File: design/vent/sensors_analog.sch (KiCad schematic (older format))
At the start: 11 parts, among them J16 Conn_01x02, J17 Conn_01x02, J18 Conn_01x03, J19 Conn_01x02, J20 Conn_01x02, U11 SPU01M-15

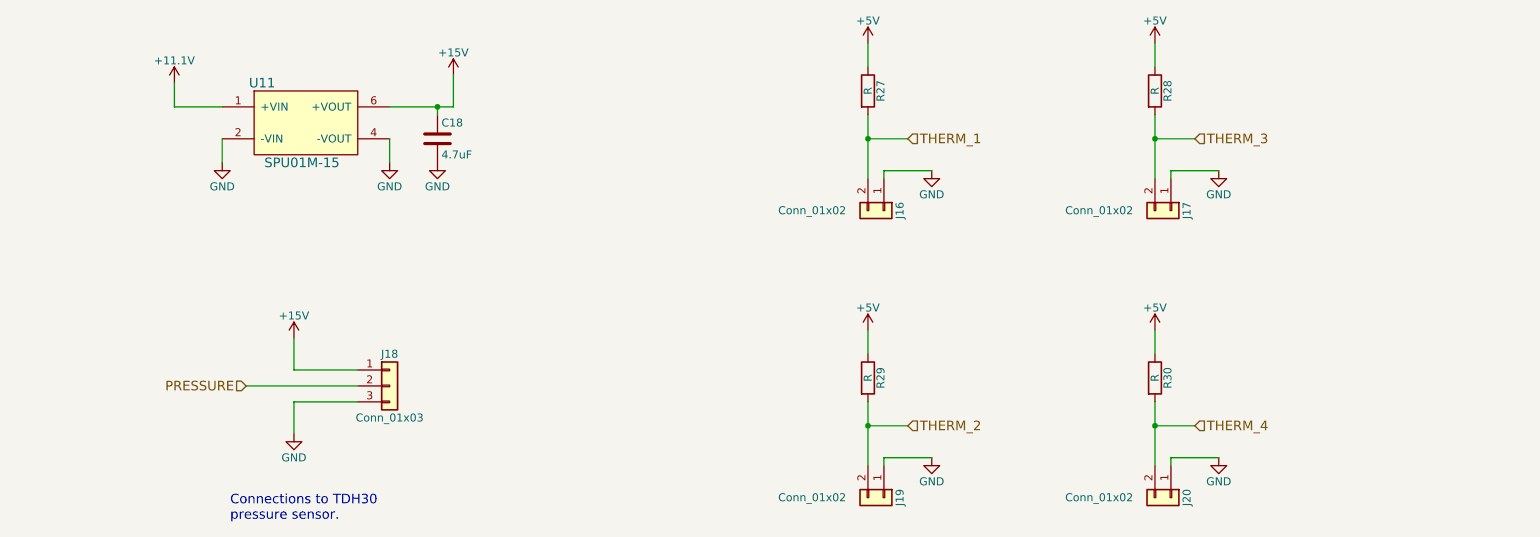
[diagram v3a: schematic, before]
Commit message: Merge control power and analog sensor connectors
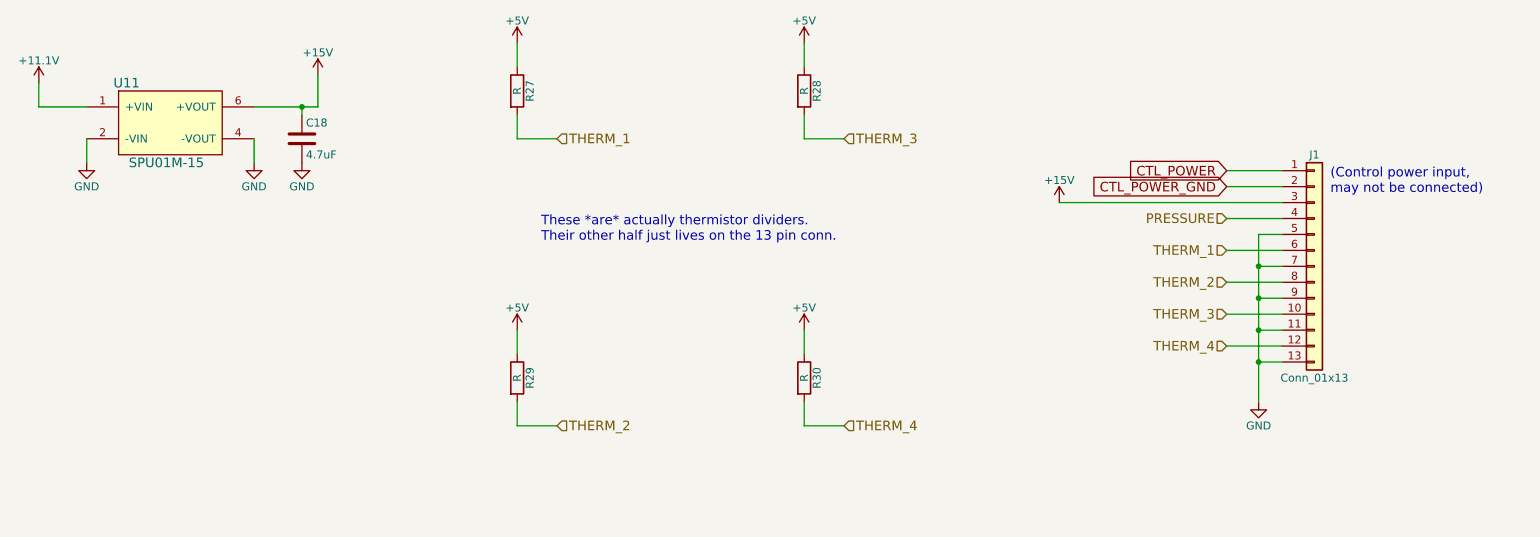
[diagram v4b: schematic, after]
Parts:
- removed J16, J17, J19, J20: Conn_01x02, Connectors_Phoenix:PhoenixContact_MCV-G_02x3.50mm_Vertical, symbol Conn_01x02
- removed J18: Conn_01x03, symbol Conn_01x03
- added J1: Conn_01x13, symbol Conn_01x13
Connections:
- net +15V: now also J1.3 (Pin_3)
- net GND: now also J1.11 (Pin_11), J1.13 (Pin_13), J1.5 (Pin_5), J1.7 (Pin_7), J1.9 (Pin_9)
- net PRESSURE: now also J1.4 (Pin_4)
- net THERM_1: now also J1.6 (Pin_6)
- net THERM_2: now also J1.8 (Pin_8)
- net THERM_3: now also J1.10 (Pin_10)
- net THERM_4: now also J1.12 (Pin_12)
- new net CTL_POWER: J1.1 (Pin_1)
- new net CTL_POWER_GND: J1.2 (Pin_2)
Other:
- note added: "(Control power input,\nmay not be connected)"
- note added: "These *are* actually thermistor dividers.\nTheir other half just lives on the 13 pin conn."
- note removed: "Connections to TDH30\npressure sensor."
- moved on the sheet: C18, R27, R28, R29, R30, U11

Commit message: Break out I2C lines on dsub connector
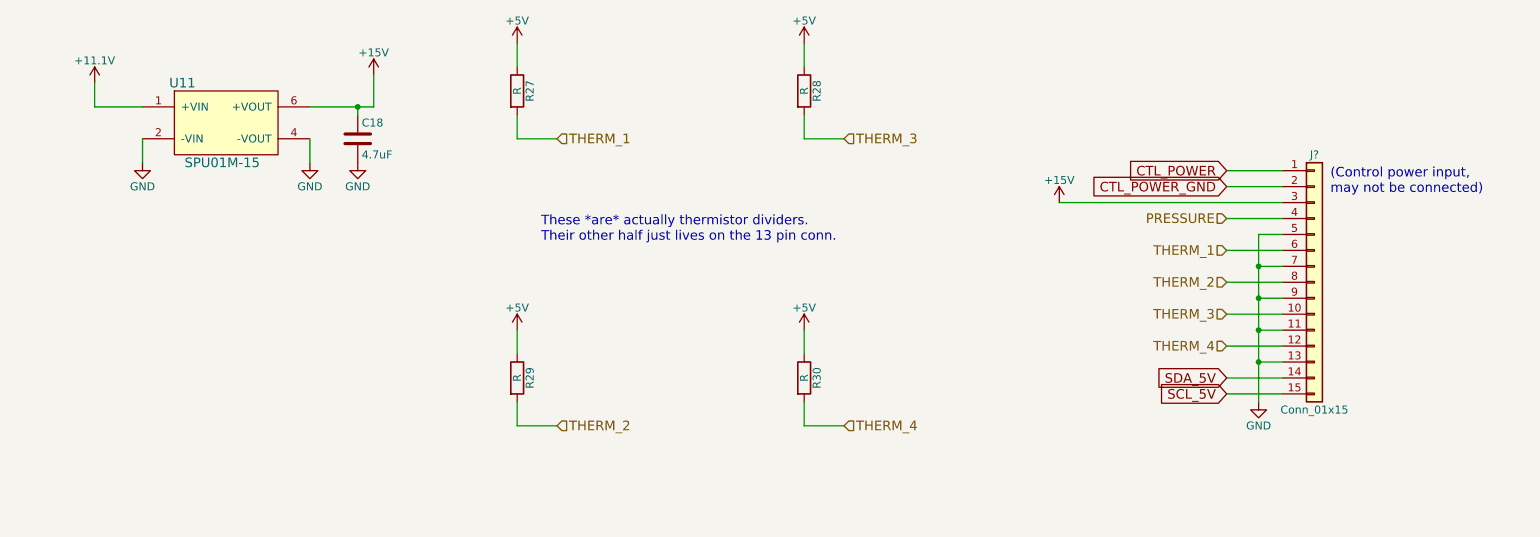
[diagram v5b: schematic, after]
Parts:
- removed J1: Conn_01x13, symbol Conn_01x13
- added J?: Conn_01x15, symbol Conn_01x15
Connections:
- net +15V: now also J?.3 (Pin_3)
- net CTL_POWER: now also J?.1 (Pin_1)
- net CTL_POWER_GND: now also J?.2 (Pin_2)
- net GND: now also J?.11 (Pin_11), J?.13 (Pin_13), J?.5 (Pin_5), J?.7 (Pin_7), J?.9 (Pin_9)
- net PRESSURE: now also J?.4 (Pin_4)
- net THERM_1: now also J?.6 (Pin_6)
- net THERM_2: now also J?.8 (Pin_8)
- net THERM_3: now also J?.10 (Pin_10)
- net THERM_4: now also J?.12 (Pin_12)
- new net SCL_5V: J?.15 (Pin_15)
- new net SDA_5V: J?.14 (Pin_14)
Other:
- moved on the sheet: C18, U11
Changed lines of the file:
@@
 L SPU01M-15 U11
 U 1 1 5AE81C3D
-P 2250 2500
-F 0 "U11" H 2050 2650 60  0000 C CNN
-F 1 "SPU01M-15" H 2300 2150 60  0000 C CNN
-F 2 "" H 2250 2500 60  0001 C CNN
-F 3 "" H 2250 2500 60  0001 C CNN
-	1    2250 2500
+P 2600 2500
+F 0 "U11" H 2400 2650 60  0000 C CNN
+F 1 "SPU01M-15" H 2650 2150 60  0000 C CNN
+F 2 "" H 2600 2500 60  0001 C CNN
+F 3 "" H 2600 2500 60  0001 C CNN
+	1    2600 2500
 	1    0    0    -1
 $EndComp
@@
 L +11.1V #PWR88
 U 1 1 5AE81C44
-P 1500 2350
-F 0 "#PWR88" H 1500 2200 50  0001 C CNN
-F 1 "+11.1V" H 1500 2490 50  0000 C CNN
-F 2 "" H 1500 2350 50  0001 C CNN
-F 3 "" H 1500 2350 50  0001 C CNN
-	1    1500 2350
-	1    0    0    -1
-$EndComp
-Wire Wire Line
-	1500 2350 1500 2500
-Wire Wire Line
-	1500 2500 1800 2500
+P 1850 2350
+F 0 "#PWR88" H 1850 2200 50  0001 C CNN
+F 1 "+11.1V" H 1850 2490 50  0000 C CNN
+F 2 "" H 1850 2350 50  0001 C CNN
+F 3 "" H 1850 2350 50  0001 C CNN
+	1    1850 2350
+	1    0    0    -1
+$EndComp
+Wire Wire Line
+	1850 2350 1850 2500
+Wire Wire Line
+	1850 2500 2150 2500
 $Comp
 L GND #PWR89
 U 1 1 5AE81C4C
-P 1800 2850
-F 0 "#PWR89" H 1800 2600 50  0001 C CNN
-F 1 "GND" H 1800 2700 50  0000 C CNN
-F 2 "" H 1800 2850 50  0001 C CNN
-F 3 "" H 1800 2850 50  0001 C CNN
-	1    1800 2850
-	1    0    0    -1
-$EndComp
-Wire Wire Line
-	1800 2850 1800 2700
+P 2150 2850
+F 0 "#PWR89" H 2150 2600 50  0001 C CNN
+F 1 "GND" H 2150 2700 50  0000 C CNN
+F 2 "" H 2150 2850 50  0001 C CNN
+F 3 "" H 2150 2850 50  0001 C CNN
+	1    2150 2850
+	1    0    0    -1
+$EndComp
+Wire Wire Line
+	2150 2850 2150 2700
 $Comp
 L GND #PWR90
 U 1 1 5AE81C53
-P 2850 2850
-F 0 "#PWR90" H 2850 2600 50  0001 C CNN
-F 1 "GND" H 2850 2700 50  0000 C CNN
-F 2 "" H 2850 2850 50  0001 C CNN
-F 3 "" H 2850 2850 50  0001 C CNN
-	1    2850 2850
-	1    0    0    -1
-$EndComp
-Wire Wire Line
-	2850 2850 2850 2700
+P 3200 2850
+F 0 "#PWR90" H 3200 2600 50  0001 C CNN
+F 1 "GND" H 3200 2700 50  0000 C CNN
+F 2 "" H 3200 2850 50  0001 C CNN
+F 3 "" H 3200 2850 50  0001 C CNN
+	1    3200 2850
+	1    0    0    -1
+$EndComp
+Wire Wire Line
+	3200 2850 3200 2700
 $Comp
 L +15V #PWR87
 U 1 1 5AE81C5A
-P 3250 2300
-F 0 "#PWR87" H 3250 2150 50  0001 C CNN
-F 1 "+15V" H 3250 2440 50  0000 C CNN
-F 2 "" H 3250 2300 50  0001 C CNN
-F 3 "" H 3250 2300 50  0001 C CNN
-	1    3250 2300
-	1    0    0    -1
-$EndComp
-Wire Wire Line
-	3250 2300 3250 2500
-Wire Wire Line
-	3250 2500 2850 2500
+P 3600 2300
+F 0 "#PWR87" H 3600 2150 50  0001 C CNN
+F 1 "+15V" H 3600 2440 50  0000 C CNN
+F 2 "" H 3600 2300 50  0001 C CNN
+F 3 "" H 3600 2300 50  0001 C CNN
+	1    3600 2300
+	1    0    0    -1
+$EndComp
+Wire Wire Line
+	3600 2300 3600 2500
+Wire Wire Line
+	3600 2500 3200 2500
 $Comp
 L R R29
@@
 L C C18
 U 1 1 5AE95521
-P 3150 2700
-F 0 "C18" H 3175 2800 50  0000 L CNN
-F 1 "4.7uF" H 3175 2600 50  0000 L CNN
-F 2 "" H 3188 2550 50  0001 C CNN
-F 3 "" H 3150 2700 50  0001 C CNN
-	1    3150 2700
+P 3500 2700
+F 0 "C18" H 3525 2800 50  0000 L CNN
+F 1 "4.7uF" H 3525 2600 50  0000 L CNN
+F 2 "" H 3538 2550 50  0001 C CNN
+F 3 "" H 3500 2700 50  0001 C CNN
+	1    3500 2700
 	1    0    0    -1
 $EndComp
@@
 L GND #PWR91
 U 1 1 5AE9556F
-P 3150 2850
-F 0 "#PWR91" H 3150 2600 50  0001 C CNN
-F 1 "GND" H 3150 2700 50  0000 C CNN
-F 2 "" H 3150 2850 50  0001 C CNN
-F 3 "" H 3150 2850 50  0001 C CNN
-	1    3150 2850
-	1    0    0    -1
-$EndComp
-Wire Wire Line
-	3150 2550 3150 2500
-Connection ~ 3150 2500
-$Comp
-L Conn_01x13 J1
-U 1 1 5AF07E70
-P 9500 3500
-F 0 "J1" H 9500 4200 50  0000 C CNN
-F 1 "Conn_01x13" H 9500 2800 50  0000 C CNN
-F 2 "" H 9500 3500 50  0001 C CNN
-F 3 "" H 9500 3500 50  0001 C CNN
-	1    9500 3500
-	1    0    0    -1
-$EndComp
+P 3500 2850
+F 0 "#PWR91" H 3500 2600 50  0001 C CNN
+F 1 "GND" H 3500 2700 50  0000 C CNN
+F 2 "" H 3500 2850 50  0001 C CNN
+F 3 "" H 3500 2850 50  0001 C CNN
+	1    3500 2850
+	1    0    0    -1
+$EndComp
+Wire Wire Line
+	3500 2550 3500 2500
+Connection ~ 3500 2500
 Text GLabel 8950 2900 0    60   Input ~ 0
 CTL_POWER
@@
 Text Notes 4650 3350 0    60   ~ 0
 These *are* actually thermistor dividers.\nTheir other half just lives on the 13 pin conn.
+$Comp
+L Conn_01x15 J?
+U 1 1 5AF0F16E
+P 9500 3600
+F 0 "J?" H 9500 4400 50  0000 C CNN
+F 1 "Conn_01x15" H 9500 2800 50  0000 C CNN
+F 2 "" H 9500 3600 50  0001 C CNN
+F 3 "" H 9500 3600 50  0001 C CNN
+	1    9500 3600
+	1    0    0    -1
+$EndComp
+Text GLabel 8950 4300 0    60   Input ~ 0
+SCL_5V
+Text GLabel 8950 4200 0    60   Input ~ 0
+SDA_5V
+Wire Wire Line
+	8950 4200 9300 4200
+Wire Wire Line
+	8950 4300 9300 4300
 $EndSCHEMATC

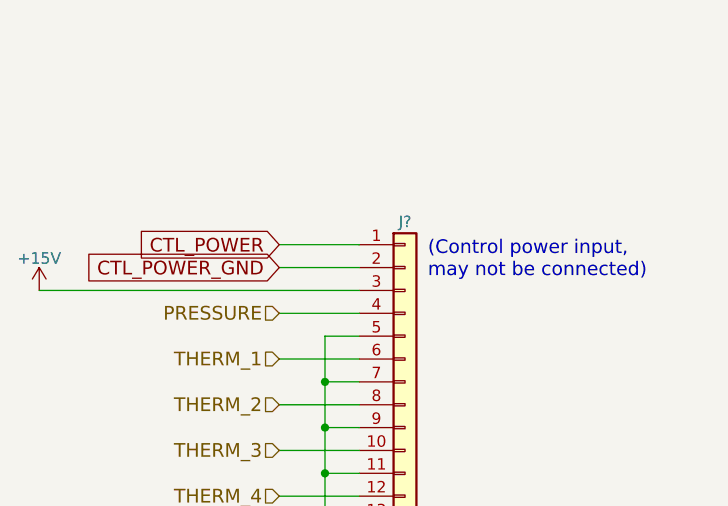
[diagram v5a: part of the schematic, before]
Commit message: Add support for injector valve default state
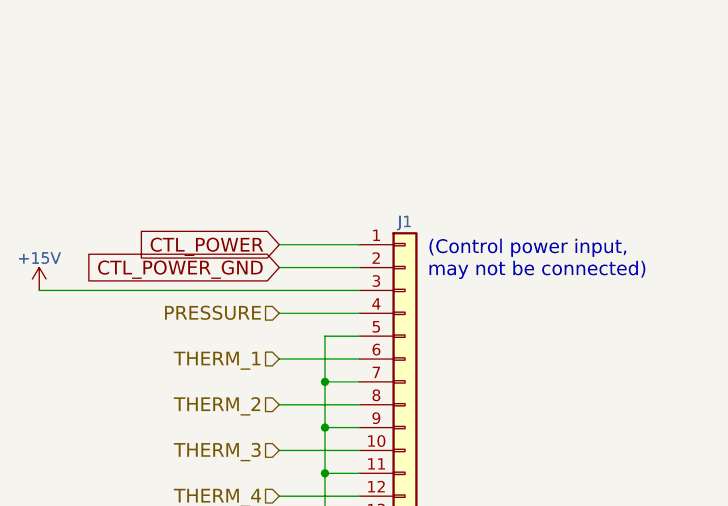
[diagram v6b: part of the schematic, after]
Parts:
- gave numbers to parts that had none: 1
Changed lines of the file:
@@
 	4750 2700 4500 2700
 $Comp
-L +5V #PWR85
+L +5V #PWR87
 U 1 1 5AE8176B
 P 4500 2100
-F 0 "#PWR85" H 4500 1950 50  0001 C CNN
+F 0 "#PWR87" H 4500 1950 50  0001 C CNN
 F 1 "+5V" H 4500 2240 50  0000 C CNN
 F 2 "" H 4500 2100 50  0001 C CNN
@@
 $EndComp
 $Comp
-L +11.1V #PWR88
+L +11.1V #PWR90
 U 1 1 5AE81C44
 P 1850 2350
-F 0 "#PWR88" H 1850 2200 50  0001 C CNN
+F 0 "#PWR90" H 1850 2200 50  0001 C CNN
 F 1 "+11.1V" H 1850 2490 50  0000 C CNN
 F 2 "" H 1850 2350 50  0001 C CNN
@@
 	1850 2500 2150 2500
 $Comp
-L GND #PWR89
+L GND #PWR91
 U 1 1 5AE81C4C
 P 2150 2850
-F 0 "#PWR89" H 2150 2600 50  0001 C CNN
+F 0 "#PWR91" H 2150 2600 50  0001 C CNN
 F 1 "GND" H 2150 2700 50  0000 C CNN
 F 2 "" H 2150 2850 50  0001 C CNN
@@
 	2150 2850 2150 2700
 $Comp
-L GND #PWR90
+L GND #PWR92
 U 1 1 5AE81C53
 P 3200 2850
-F 0 "#PWR90" H 3200 2600 50  0001 C CNN
+F 0 "#PWR92" H 3200 2600 50  0001 C CNN
 F 1 "GND" H 3200 2700 50  0000 C CNN
 F 2 "" H 3200 2850 50  0001 C CNN
@@
 	3200 2850 3200 2700
 $Comp
-L +15V #PWR87
+L +15V #PWR89
 U 1 1 5AE81C5A
 P 3600 2300
-F 0 "#PWR87" H 3600 2150 50  0001 C CNN
+F 0 "#PWR89" H 3600 2150 50  0001 C CNN
 F 1 "+15V" H 3600 2440 50  0000 C CNN
 F 2 "" H 3600 2300 50  0001 C CNN
@@
 	4750 4500 4500 4500
 $Comp
-L +5V #PWR93
+L +5V #PWR95
 U 1 1 5AE82545
 P 4500 3900
-F 0 "#PWR93" H 4500 3750 50  0001 C CNN
+F 0 "#PWR95" H 4500 3750 50  0001 C CNN
 F 1 "+5V" H 4500 4040 50  0000 C CNN
 F 2 "" H 4500 3900 50  0001 C CNN
@@
 	6550 2700 6300 2700
 $Comp
-L +5V #PWR86
+L +5V #PWR88
 U 1 1 5AE825E4
 P 6300 2100
-F 0 "#PWR86" H 6300 1950 50  0001 C CNN
+F 0 "#PWR88" H 6300 1950 50  0001 C CNN
 F 1 "+5V" H 6300 2240 50  0000 C CNN
 F 2 "" H 6300 2100 50  0001 C CNN
@@
 	6550 4500 6300 4500
 $Comp
-L +5V #PWR94
+L +5V #PWR96
 U 1 1 5AE8265D
 P 6300 3900
-F 0 "#PWR94" H 6300 3750 50  0001 C CNN
+F 0 "#PWR96" H 6300 3750 50  0001 C CNN
 F 1 "+5V" H 6300 4040 50  0000 C CNN
 F 2 "" H 6300 3900 50  0001 C CNN
@@
 $EndComp
 $Comp
-L GND #PWR91
+L GND #PWR93
 U 1 1 5AE9556F
 P 3500 2850
-F 0 "#PWR91" H 3500 2600 50  0001 C CNN
+F 0 "#PWR93" H 3500 2600 50  0001 C CNN
 F 1 "GND" H 3500 2700 50  0000 C CNN
 F 2 "" H 3500 2850 50  0001 C CNN
@@
 (Control power input,\nmay not be connected)
 $Comp
-L +15V #PWR92
+L +15V #PWR94
 U 1 1 5AF096B4
 P 7900 3100
-F 0 "#PWR92" H 7900 2950 50  0001 C CNN
+F 0 "#PWR94" H 7900 2950 50  0001 C CNN
 F 1 "+15V" H 7900 3240 50  0000 C CNN
 F 2 "" H 7900 3100 50  0001 C CNN
@@
 	8950 4000 9300 4000
 $Comp
-L GND #PWR96
+L GND #PWR97
 U 1 1 5AF0A90A
 P 9150 4350
-F 0 "#PWR96" H 9150 4100 50  0001 C CNN
+F 0 "#PWR97" H 9150 4100 50  0001 C CNN
 F 1 "GND" H 9150 4200 50  0000 C CNN
 F 2 "" H 9150 4350 50  0001 C CNN
@@
 These *are* actually thermistor dividers.\nTheir other half just lives on the 13 pin conn.
 $Comp
-L Conn_01x15 J?
+L Conn_01x15 J1
 U 1 1 5AF0F16E
 P 9500 3600
-F 0 "J?" H 9500 4400 50  0000 C CNN
+F 0 "J1" H 9500 4400 50  0000 C CNN
 F 1 "Conn_01x15" H 9500 2800 50  0000 C CNN
 F 2 "" H 9500 3600 50  0001 C CNN

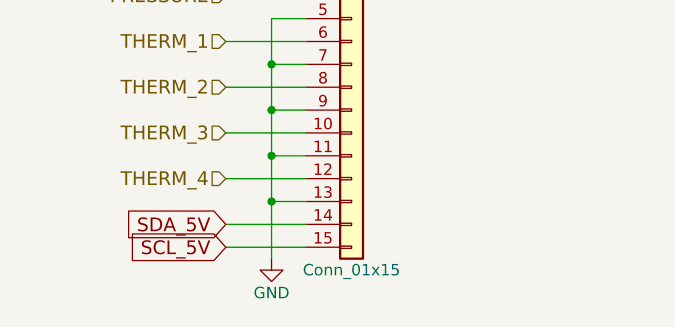
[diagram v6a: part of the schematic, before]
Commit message: Add connector part numbers to schematic
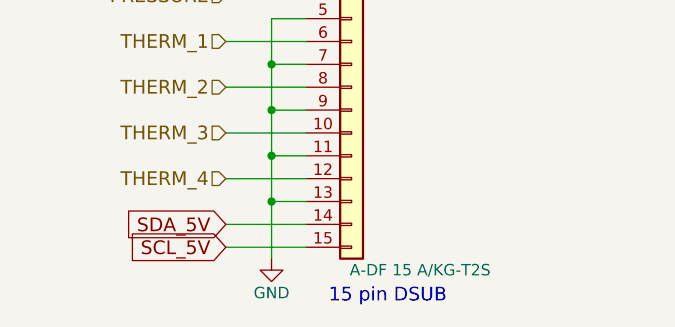
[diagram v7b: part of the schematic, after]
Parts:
- C18: footprint (none) -> Diode_SMD:D_0805_2012Metric_Pad0.97x1.50mm_HandSolder
- J1: value Conn_01x15 -> A-DF 15 A/KG-T2S; footprint (none) -> Connector_Dsub:DSUB-15_Male_Horizontal_P2.77x2.84mm_EdgePinOffset7.70mm_Housed_MountingHolesOffset9.12mm
- R27, R28, R29, R30: footprint Resistors_ThroughHole:R_Axial_DIN0207_L6.3mm_D2.5mm_P10.16mm_Horizontal -> Resistors_SMD:R_0805_HandSoldering
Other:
- note added: "15 pin DSUB"
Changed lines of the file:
@@
 F 0 "R27" V 4580 2400 50  0000 C CNN
 F 1 "R" V 4500 2400 50  0000 C CNN
-F 2 "Resistors_ThroughHole:R_Axial_DIN0207_L6.3mm_D2.5mm_P10.16mm_Horizontal" V 4430 2400 50  0001 C CNN
+F 2 "Resistors_SMD:R_0805_HandSoldering" V 4430 2400 50  0001 C CNN
 F 3 "" H 4500 2400 50  0001 C CNN
 	1    4500 2400
@@
 	4750 2700 4500 2700
 $Comp
-L +5V #PWR87
+L +5V #PWR087
 U 1 1 5AE8176B
 P 4500 2100
-F 0 "#PWR87" H 4500 1950 50  0001 C CNN
+F 0 "#PWR087" H 4500 1950 50  0001 C CNN
 F 1 "+5V" H 4500 2240 50  0000 C CNN
 F 2 "" H 4500 2100 50  0001 C CNN
@@
 $EndComp
 $Comp
-L +11.1V #PWR90
+L +11.1V #PWR088
 U 1 1 5AE81C44
 P 1850 2350
-F 0 "#PWR90" H 1850 2200 50  0001 C CNN
+F 0 "#PWR088" H 1850 2200 50  0001 C CNN
 F 1 "+11.1V" H 1850 2490 50  0000 C CNN
 F 2 "" H 1850 2350 50  0001 C CNN
@@
 	1850 2500 2150 2500
 $Comp
-L GND #PWR91
+L GND #PWR089
 U 1 1 5AE81C4C
 P 2150 2850
-F 0 "#PWR91" H 2150 2600 50  0001 C CNN
+F 0 "#PWR089" H 2150 2600 50  0001 C CNN
 F 1 "GND" H 2150 2700 50  0000 C CNN
 F 2 "" H 2150 2850 50  0001 C CNN
@@
 	2150 2850 2150 2700
 $Comp
-L GND #PWR92
+L GND #PWR090
 U 1 1 5AE81C53
 P 3200 2850
-F 0 "#PWR92" H 3200 2600 50  0001 C CNN
+F 0 "#PWR090" H 3200 2600 50  0001 C CNN
 F 1 "GND" H 3200 2700 50  0000 C CNN
 F 2 "" H 3200 2850 50  0001 C CNN
@@
 	3200 2850 3200 2700
 $Comp
-L +15V #PWR89
+L +15V #PWR091
 U 1 1 5AE81C5A
 P 3600 2300
-F 0 "#PWR89" H 3600 2150 50  0001 C CNN
+F 0 "#PWR091" H 3600 2150 50  0001 C CNN
 F 1 "+15V" H 3600 2440 50  0000 C CNN
 F 2 "" H 3600 2300 50  0001 C CNN
@@
 F 0 "R29" V 4580 4200 50  0000 C CNN
 F 1 "R" V 4500 4200 50  0000 C CNN
-F 2 "Resistors_ThroughHole:R_Axial_DIN0207_L6.3mm_D2.5mm_P10.16mm_Horizontal" V 4430 4200 50  0001 C CNN
+F 2 "Resistors_SMD:R_0805_HandSoldering" V 4430 4200 50  0001 C CNN
 F 3 "" H 4500 4200 50  0001 C CNN
 	1    4500 4200
@@
 	4750 4500 4500 4500
 $Comp
-L +5V #PWR95
+L +5V #PWR092
 U 1 1 5AE82545
 P 4500 3900
-F 0 "#PWR95" H 4500 3750 50  0001 C CNN
+F 0 "#PWR092" H 4500 3750 50  0001 C CNN
 F 1 "+5V" H 4500 4040 50  0000 C CNN
 F 2 "" H 4500 3900 50  0001 C CNN
@@
 F 0 "R28" V 6380 2400 50  0000 C CNN
 F 1 "R" V 6300 2400 50  0000 C CNN
-F 2 "Resistors_ThroughHole:R_Axial_DIN0207_L6.3mm_D2.5mm_P10.16mm_Horizontal" V 6230 2400 50  0001 C CNN
+F 2 "Resistors_SMD:R_0805_HandSoldering" V 6230 2400 50  0001 C CNN
 F 3 "" H 6300 2400 50  0001 C CNN
 	1    6300 2400
@@
 	6550 2700 6300 2700
 $Comp
-L +5V #PWR88
+L +5V #PWR093
 U 1 1 5AE825E4
 P 6300 2100
-F 0 "#PWR88" H 6300 1950 50  0001 C CNN
+F 0 "#PWR093" H 6300 1950 50  0001 C CNN
 F 1 "+5V" H 6300 2240 50  0000 C CNN
 F 2 "" H 6300 2100 50  0001 C CNN
@@
 F 0 "R30" V 6380 4200 50  0000 C CNN
 F 1 "R" V 6300 4200 50  0000 C CNN
-F 2 "Resistors_ThroughHole:R_Axial_DIN0207_L6.3mm_D2.5mm_P10.16mm_Horizontal" V 6230 4200 50  0001 C CNN
+F 2 "Resistors_SMD:R_0805_HandSoldering" V 6230 4200 50  0001 C CNN
 F 3 "" H 6300 4200 50  0001 C CNN
 	1    6300 4200
@@
 	6550 4500 6300 4500
 $Comp
-L +5V #PWR96
+L +5V #PWR094
 U 1 1 5AE8265D
 P 6300 3900
-F 0 "#PWR96" H 6300 3750 50  0001 C CNN
+F 0 "#PWR094" H 6300 3750 50  0001 C CNN
 F 1 "+5V" H 6300 4040 50  0000 C CNN
 F 2 "" H 6300 3900 50  0001 C CNN
@@
 F 0 "C18" H 3525 2800 50  0000 L CNN
 F 1 "4.7uF" H 3525 2600 50  0000 L CNN
-F 2 "" H 3538 2550 50  0001 C CNN
+F 2 "Diode_SMD:D_0805_2012Metric_Pad0.97x1.50mm_HandSolder" H 3538 2550 50  0001 C CNN
 F 3 "" H 3500 2700 50  0001 C CNN
 	1    3500 2700
@@
 $EndComp
 $Comp
-L GND #PWR93
+L GND #PWR095
 U 1 1 5AE9556F
 P 3500 2850
-F 0 "#PWR93" H 3500 2600 50  0001 C CNN
+F 0 "#PWR095" H 3500 2600 50  0001 C CNN
 F 1 "GND" H 3500 2700 50  0000 C CNN
 F 2 "" H 3500 2850 50  0001 C CNN
@@
 (Control power input,\nmay not be connected)
 $Comp
-L +15V #PWR94
+L +15V #PWR096
 U 1 1 5AF096B4
 P 7900 3100
-F 0 "#PWR94" H 7900 2950 50  0001 C CNN
+F 0 "#PWR096" H 7900 2950 50  0001 C CNN
 F 1 "+15V" H 7900 3240 50  0000 C CNN
 F 2 "" H 7900 3100 50  0001 C CNN
@@
 	8950 4000 9300 4000
 $Comp
-L GND #PWR97
+L GND #PWR097
 U 1 1 5AF0A90A
 P 9150 4350
-F 0 "#PWR97" H 9150 4100 50  0001 C CNN
+F 0 "#PWR097" H 9150 4100 50  0001 C CNN
 F 1 "GND" H 9150 4200 50  0000 C CNN
 F 2 "" H 9150 4350 50  0001 C CNN
@@
 P 9500 3600
 F 0 "J1" H 9500 4400 50  0000 C CNN
-F 1 "Conn_01x15" H 9500 2800 50  0000 C CNN
-F 2 "" H 9500 3600 50  0001 C CNN
+F 1 "A-DF 15 A/KG-T2S" H 9800 2800 50  0000 C CNN
+F 2 "Connector_Dsub:DSUB-15_Male_Horizontal_P2.77x2.84mm_EdgePinOffset7.70mm_Housed_MountingHolesOffset9.12mm" H 9500 3600 50  0001 C CNN
 F 3 "" H 9500 3600 50  0001 C CNN
 	1    9500 3600
@@
 Wire Wire Line
 	8950 4300 9300 4300
+Text Notes 9400 4550 0    60   ~ 0
+15 pin DSUB
 $EndSCHEMATC

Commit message: Add barrier block footprints
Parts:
- U11: footprint (none) -> Flight_Instr:SIP6_Housing
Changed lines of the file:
@@
 F 0 "U11" H 2400 2650 60  0000 C CNN
 F 1 "SPU01M-15" H 2650 2150 60  0000 C CNN
-F 2 "" H 2600 2500 60  0001 C CNN
+F 2 "Flight_Instr:SIP6_Housing" H 2600 2500 60  0001 C CNN
 F 3 "" H 2600 2500 60  0001 C CNN
 	1    2600 2500
